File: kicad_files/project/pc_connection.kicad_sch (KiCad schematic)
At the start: 19 parts, among them U4 U241-041N-1WR85-1_C2880605, U5 FT232H

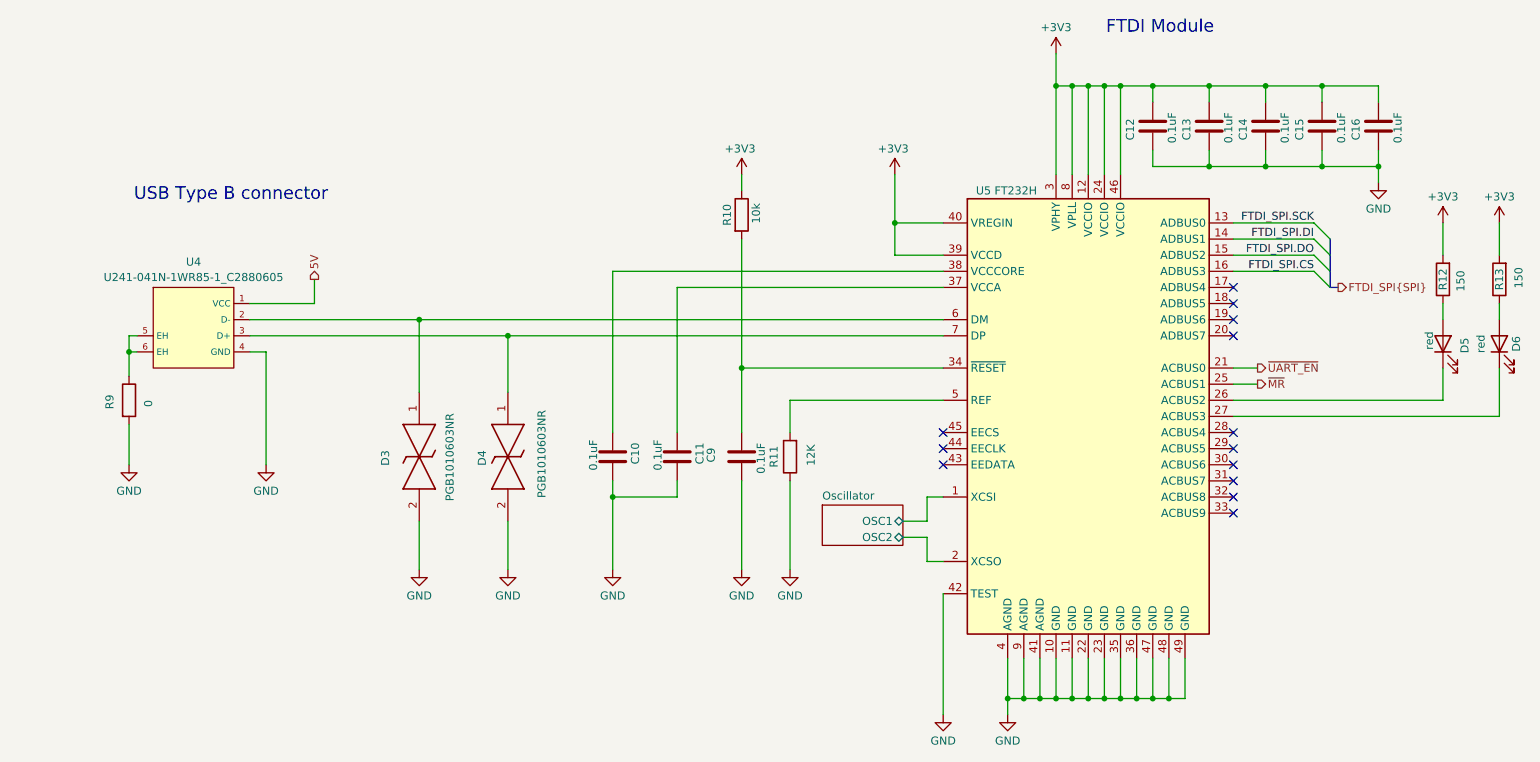
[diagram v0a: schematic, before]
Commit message: started with board layout, also added more stuff on the schematic
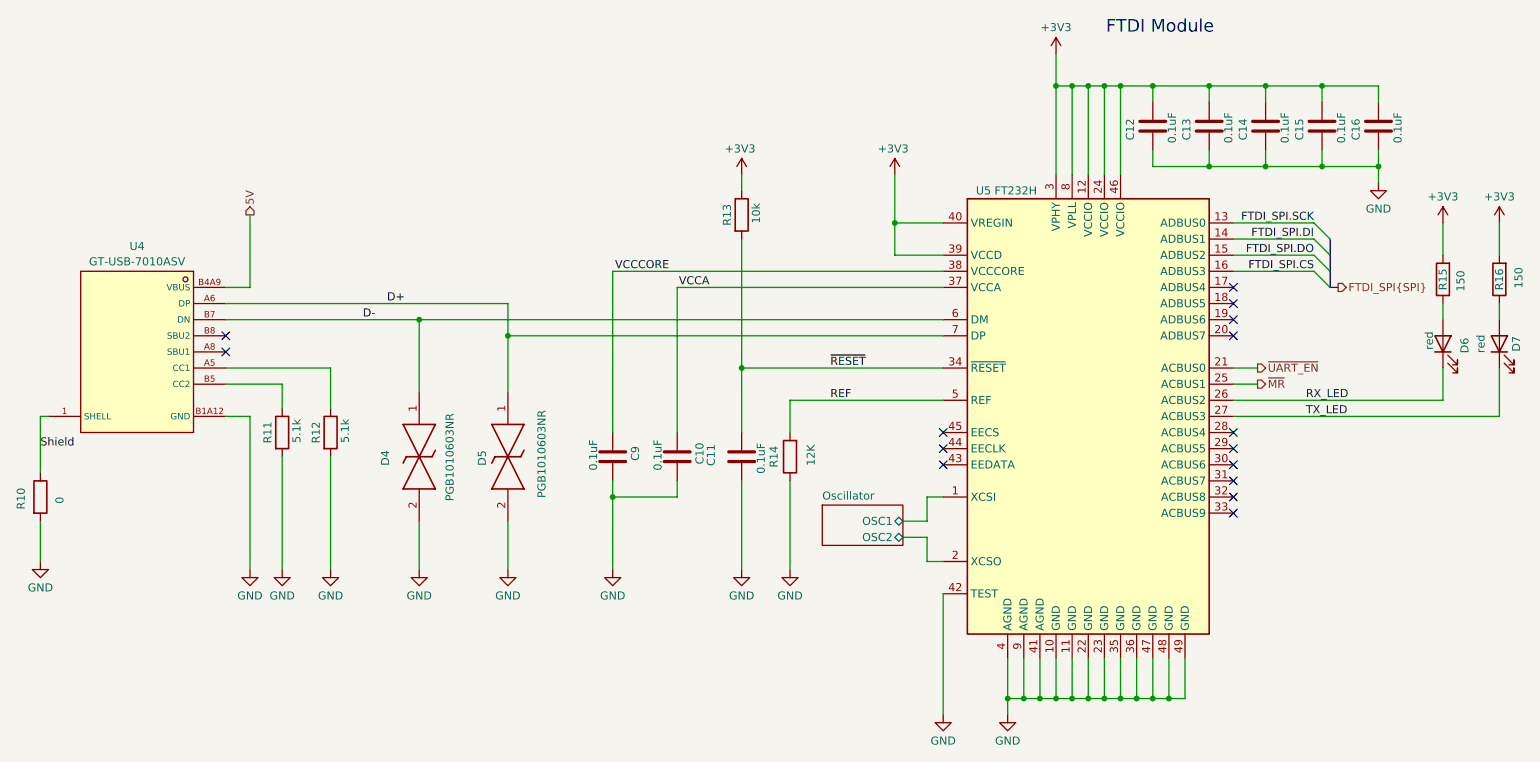
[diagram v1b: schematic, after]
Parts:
- removed R9: 0, Resistor_SMD:R_0805_2012Metric, symbol Device:R
- removed U4: U241-041N-1WR85-1_C2880605, easy_eda:USB-B-TH_AMPHENOL_61729-0010BLF, symbol easy_eda:U241-041N-1WR85-1_C2880605
- added R10: 0, Resistor_SMD:R_0805_2012Metric, symbol Device:R
- added R11, R12: 5.1k, Resistor_SMD:R_0805_2012Metric, symbol Device:R
- added U4: GT-USB-7010ASV, easy_eda:USB-C-SMD_G-SWITCH_GT-USB-7010ASV, symbol easy_eda:GT-USB-7010ASV
- renumbered C11 to C10, C9 to C11, C10 to C9, D3 to D4, D4 to D5, D5 to D6, D6 to D7, R10 to R13, R11 to R14, R12 to R15, R13 to R16
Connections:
- net 5V: now also U4.A4B9 (VBUS), U4.B4A9 (VBUS)
- net GND: now also R10.2, R11.2, R12.2, U4.A1B12 (GND), U4.B1A12 (GND)
- net ~{RESET}: now reaches C11.2, R13.2, U5.34 (~{RESET})
- net D-: now reaches D4.1, U5.6 (DM)
- net D-: now also U4.A7 (DN1), U4.B7 (DN)
- net D+: now reaches D5.1, U5.7 (DP)
- net D+: now also U4.A6 (DP), U4.B6 (DP2)
- net VCCCORE: now reaches C9.1, U5.38 (VCCCORE)
- net VCCA: now reaches C10.1, U5.37 (VCCA)
- net RX_LED: now reaches D6.1 (K), U5.26 (ACBUS2)
- net TX_LED: now reaches D7.1 (K), U5.27 (ACBUS3)
- net REF: now reaches R14.2, U5.5 (REF)
- new net: R11.1, U4.B5 (CC2)
- new net: R12.1, U4.A5 (CC1)
- new net Shield: R10.1, U4.1 (SHELL), U4.2 (SHELL), U4.3 (SHELL), U4.4 (SHELL)
- no-connect marks 13 -> 15
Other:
- note removed: "USB Type B connector"

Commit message: misc: simplifiy power pins and other components, add test pins
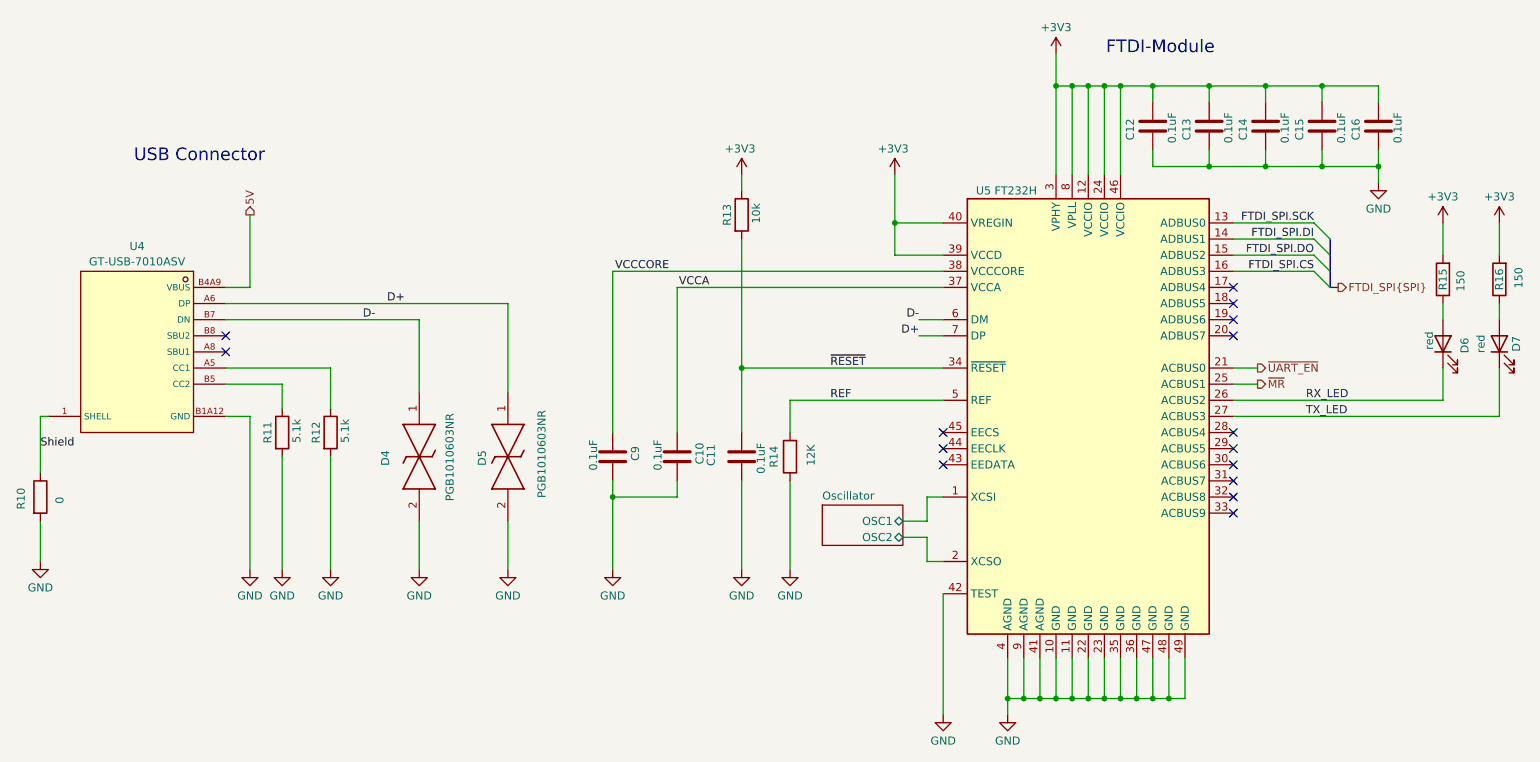
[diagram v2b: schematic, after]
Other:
- note added: "FTDI-Module"
- note added: "USB Connector"
- note removed: "FTDI Module"
- title: (none) -> PC connection
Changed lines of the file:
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@@
 	(paper "A4")
 	(title_block
+		(title "PC connection")
 		(date "2024-05-30")
 		(rev "0.1")
@@
 	)
 	(junction
-		(at 91.44 88.9)
-		(diameter 0)
-		(color 0 0 0 0)
-	)
-	(junction
 		(at 201.93 52.07)
 		(diameter 0)
@@
 	(junction
 		(at 204.47 148.59)
-		(diameter 0)
-		(color 0 0 0 0)
-	)
-	(junction
-		(at 105.41 91.44)
 		(diameter 0)
 		(color 0 0 0 0)
@@
 	(wire
 		(pts
-			(xy 105.41 91.44) (xy 173.99 91.44)
-		)
-		(stroke
-			(width 0)
-			(type default)
-		)
-	)
-	(wire
-		(pts
 			(xy 69.85 110.49) (xy 69.85 128.27)
 		)
@@
 	(wire
 		(pts
-			(xy 91.44 88.9) (xy 173.99 88.9)
-		)
-		(stroke
-			(width 0)
-			(type default)
-		)
-	)
-	(wire
-		(pts
 			(xy 167.64 123.19) (xy 171.45 123.19)
 		)
@@
 	(wire
 		(pts
+			(xy 170.18 91.44) (xy 173.99 91.44)
+		)
+		(stroke
+			(width 0)
+			(type default)
+		)
+	)
+	(wire
+		(pts
 			(xy 215.9 54.61) (xy 215.9 52.07)
 		)
@@
 	(wire
 		(pts
-			(xy 105.41 86.36) (xy 105.41 91.44)
+			(xy 105.41 86.36) (xy 105.41 100.33)
 		)
 		(stroke
@@
 	(wire
 		(pts
+			(xy 170.18 88.9) (xy 173.99 88.9)
+		)
+		(stroke
+			(width 0)
+			(type default)
+		)
+	)
+	(wire
+		(pts
 			(xy 194.31 148.59) (xy 196.85 148.59)
 		)
@@
 	(wire
 		(pts
-			(xy 105.41 91.44) (xy 105.41 100.33)
-		)
-		(stroke
-			(width 0)
-			(type default)
-		)
-	)
-	(wire
-		(pts
 			(xy 232.41 73.66) (xy 219.71 73.66)
 		)
@@
 		)
 	)
-	(text "FTDI Module\n\n"
+	(text "USB Connector"
+		(exclude_from_sim no)
+		(at 46.482 64.262 0)
+		(effects
+			(font
+				(size 2 2)
+			)
+			(justify left bottom)
+		)
+	)
+	(text "FTDI-Module\n"
 		(exclude_from_sim no)
 		(at 199.644 47.244 0)
@@
 		)
 	)
+	(label "D+"
+		(at 170.18 91.44 180)
+		(fields_autoplaced yes)
+		(effects
+			(font
+				(size 1.27 1.27)
+			)
+			(justify right bottom)
+		)
+	)
 	(label "RX_LED"
 		(at 231.14 101.6 0)
@@
 		(fields_autoplaced yes)
 		(effects
+			(font
+				(size 1.27 1.27)
+			)
+			(justify right bottom)
+		)
+	)
+	(label "D-"
+		(at 170.18 88.9 180)
+		(fields_autoplaced yes)
+		(effects
